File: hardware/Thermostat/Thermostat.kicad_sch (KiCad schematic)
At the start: 54 parts, among them J1 Barrel_Jack_Switch, J2 Screw_Terminal_01x02, J3 AVR-ISP-6, J4 MainConnectorr, K1 G6E, K2 G6E, K3 G6E, K4 G6E, SW1 12MM, SW2 12MM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

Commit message: WIP
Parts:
- removed BT1: Battery_Cell, Battery:BatteryHolder_Keystone_1058_1x2032, symbol Device:Battery_Cell
- removed C7, C8: 0.1uF, Capacitor_SMD:C_0603_1608Metric, symbol Device:C
- removed J2: Screw_Terminal_01x02, TerminalBlock_MetzConnect:TerminalBlock_MetzConnect_Type094_RT03502HBLU_1x02_P5.00mm_Horizontal, symbol Connector:Screw_Terminal_01x02
- removed U7: THVD1500, Package_SO:SOIC-8_3.9x4.9mm_P1.27mm, symbol Interface_UART:THVD1500
- added J2: Conn_01x02_Pin, Connector_PinHeader_2.54mm:PinHeader_1x02_P2.54mm_Vertical_SMD_Pin1Left, symbol Connector:Conn_01x02_Pin
- added U2: 47L04, Package_SO:SOIC-8_3.9x4.9mm_P1.27mm, symbol Memory_NVRAM:47L04
- Y1: footprint Crystal:Crystal_SMD_HC49-SD -> Crystal:Crystal_SMD_5032-2Pin_5.0x3.2mm
- Y2: footprint ThermostatFootprints:MC-306_EPS -> Crystal:Crystal_SMD_5032-2Pin_5.0x3.2mm
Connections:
- net +BATT is gone; now on net +5V: U8.8 (VCC)
- net +5V: no longer U8.3 (VBAT)
- net GND: now also SW2.1, U8.3 (VBAT); no longer SW2.2
- net RX0: now also J2.2 (Pin_2)
- net TX0: now also J2.1 (Pin_1)
- net at U5.32 (PD2): now also SW2.2; no longer SW2.1
- no-connect marks 20 -> 18

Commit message: Wip
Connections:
- net at D4.2 (A), U3.4 (IN4): now also U5.22 (ADC7); no longer U5.14 (PB2)
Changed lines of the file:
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@@
-	)
-	(no_connect
-		(at 20.32 118.11)
 	)
 	(no_connect
@@
 	)
 	(no_connect
+		(at 50.8 115.57)
+	)
+	(no_connect
 		(at 50.8 110.49)
 	)
@@
 	(wire
 		(pts
+			(xy 16.51 90.17) (xy 16.51 118.11)
+		)
+		(stroke
+			(width 0)
+			(type default)
+		)
+	)
+	(wire
+		(pts
 			(xy 50.8 190.5) (xy 64.77 190.5)
 		)
@@
 	(wire
 		(pts
-			(xy 64.77 115.57) (xy 50.8 115.57)
+			(xy 16.51 118.11) (xy 20.32 118.11)
 		)
 		(stroke
@@
 	(wire
 		(pts
+			(xy 45.72 101.6) (xy 45.72 90.17)
+		)
+		(stroke
+			(width 0)
+			(type default)
+		)
+	)
+	(wire
+		(pts
 			(xy 193.04 29.21) (xy 209.55 29.21)
 		)
@@
 	(wire
 		(pts
+			(xy 64.77 101.6) (xy 64.77 138.43)
+		)
+		(stroke
+			(width 0)
+			(type default)
+		)
+	)
+	(wire
+		(pts
 			(xy 195.58 104.14) (xy 195.58 95.25)
 		)
@@
 	(wire
 		(pts
-			(xy 64.77 138.43) (xy 64.77 115.57)
-		)
-		(stroke
-			(width 0)
-			(type default)
-		)
-	)
-	(wire
-		(pts
 			(xy 158.75 77.47) (xy 158.75 82.55)
 		)
@@
 	(wire
 		(pts
+			(xy 64.77 101.6) (xy 45.72 101.6)
+		)
+		(stroke
+			(width 0)
+			(type default)
+		)
+	)
+	(wire
+		(pts
 			(xy 93.98 111.76) (xy 93.98 115.57)
 		)
@@
 		(pts
 			(xy 229.87 26.67) (xy 259.08 26.67)
+		)
+		(stroke
+			(width 0)
+			(type default)
+		)
+	)
+	(wire
+		(pts
+			(xy 45.72 90.17) (xy 16.51 90.17)
 		)
 		(stroke
@@
 			(justify left bottom)
 		)
-		(property "Netclass" "Power"
+		(property "Netclass" "MegaPower"
 			(at 146.7485 58.42 0)
 			(effects
@@
 			(justify left bottom)
 		)
-		(property "Netclass" "Power"
+		(property "Netclass" "MegaPower"
 			(at 128.9685 53.34 0)
 			(effects
@@
 			(justify left bottom)
 		)
-		(property "Netclass" "Power"
+		(property "Netclass" "MegaPower"
 			(at 137.8585 55.88 0)
 			(effects
@@
 			(justify left bottom)
 		)
-		(property "Netclass" "Power"
+		(property "Netclass" "MegaPower"
 			(at 126.4285 63.5 0)
 			(effects

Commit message: WIP
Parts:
- removed D1, D2, D3, D4: LED, LED_SMD:LED_0805_2012Metric, symbol Device:LED
- removed D5: SM6T27A, Diode_SMD:D_SMB, symbol Diode:SM6T27A
- removed R2, R3, R4, R5: 660, Resistor_SMD:R_0603_1608Metric, symbol Device:R_US
- removed S1: 2MS1T1B1M2QES, ThermostatFootprints:2MS1T1B1M2QES, symbol ThermoSymbols:2MS3T1B1M2QES
- removed S3: 2MS1T1B1M2QES, ThermostatFootprints:2MS1T1B1M2QES, symbol ThermoSymbols:2MS1T1B1M2QES
- removed Y2: Crystal_GND23, Crystal:Crystal_SMD_5032-2Pin_5.0x3.2mm, symbol Device:Crystal_GND23
- added C7: C, Capacitor_SMD:C_0603_1608Metric, symbol Device:C
- added D5: 1N4007, Diode_THT:D_DO-41_SOD81_P10.16mm_Horizontal, symbol Diode:1N4007
- added SW7, SW9: 12MM, ThermostatFootprints:B3F, symbol Switch:SW_Push
- added Y3: Crystal, Crystal:Crystal_SMD_5032-2Pin_5.0x3.2mm, symbol Device:Crystal
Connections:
- net +5V: now also U1.6 (^RESET), U2.8 (VCC)
- net 24VDC: now also D5.1 (K); no longer J1.1
- net GND: now also U2.2 (A1), U2.3 (A2), U2.4 (VSS), C7.2, SW7.2, SW9.2
- net I2C_SCL: now also U2.6 (SCL)
- net I2C_SDA: now also U2.5 (SDA)
- net ^RESET: no longer U1.6 (^RESET)
- net at U8.1 (X1): now also Y3.2
- net at U8.2 (X2): now also Y3.1
- net at SW3.1: now also U5.9 (PD5); no longer U5.11 (PD7)
- net at U2.1 (VCAP): now also C7.1
- net at U5.10 (PD6): now also SW9.1
- net at K1.1: now also U3.13 (OUT4); no longer U3.16 (OUT1)
- net at K2.1: now also U3.14 (OUT3); no longer U3.15 (OUT2)
- net at K3.1: now also U3.15 (OUT2); no longer U3.14 (OUT3)
- net at K4.1: now also U3.16 (OUT1); no longer U3.13 (OUT4)
- new net: D5.2 (A), J1.1
- new net: SW7.1, U5.11 (PD7)
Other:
- note added: "FAN ON/AUTO"
- note added: "HEAT/COOL"
- note added: "SELECT"
- note removed: "COOL"
- note removed: "FAN ON"
- note removed: "HEAT"
- note removed: "Should be 2MS3T1B1M2QES"
- moved on the sheet: C9, H1, H2, H3, H4, R1, R6, R7, SW3, SW5, U1, U2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

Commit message: WIP
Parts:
- removed U6: TMP116xxDRV, Package_SON:WSON-6-1EP_2x2mm_P0.65mm_EP1x1.6mm_ThermalVias, symbol Sensor_Temperature:TMP116xxDRV
- added C10, C8: 0.1uF, Capacitor_SMD:C_0603_1608Metric, symbol Device:C
- added U9: SHT4x, Sensor_Humidity:Sensirion_DFN-4_1.5x1.5mm_P0.8mm_SHT4x_NoCentralPad, symbol Sensor_Humidity:SHT4x
- C7: value C -> 6.8uF
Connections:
- net +5V: now also C9.2, C10.1, C8.2, U9.3 (VDD); no longer C9.1
- net GND: now also C9.1, C10.2, C8.1, U9.4 (VSS); no longer C9.2
- net I2C_SCL: now also U9.2 (SCL)
- net I2C_SDA: now also U9.1 (SDA)
- no-connect marks 18 -> 17

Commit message: Wiring / DRC / JLCPCB
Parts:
- removed U5: ATmega88-20A, Package_QFP:TQFP-32_7x7mm_P0.8mm, symbol MCU_Microchip_ATmega:ATmega88-20A
- added U5: ATmega168P-20A, Package_QFP:TQFP-32_7x7mm_P0.8mm, symbol MCU_Microchip_ATmega:ATmega168P-20A
- C1, C2, C3: footprint Capacitor_SMD:C_0603_1608Metric -> Capacitor_SMD:C_1808_4520Metric
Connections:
- net +5V: now also U5.4 (VCC), U5.6 (VCC)
- net GND: now also U5.18 (AVCC), U5.20 (AREF), U5.21 (GND), U5.3 (GND), U5.5 (GND)
- net I2C_SCL: now also U5.28 (PC5)
- net I2C_SDA: now also U5.27 (PC4)
- net RX0: now also U5.30 (PD0)
- net TX0: now also U5.31 (PD1)
- net ^RESET: now also U5.29 (~{RESET}/PC6)
- net at SW3.1: now also U5.9 (PD5)
- net at C4.2, Y1.2: now also U5.7 (XTAL1/PB6)
- net at SW4.1: now also U5.26 (PC3)
- net at C5.2, Y1.1: now also U5.8 (XTAL2/PB7)
- net at SW1.1: now also U5.1 (PD3)
- net at SW9.1: now also U5.10 (PD6)
- net at SW7.1: now also U5.11 (PD7)
- net at J3.4 (MOSI): now also U5.15 (PB3)
- net at J3.1 (MISO): now also U5.16 (PB4)
- net at J3.3 (SCK): now also U5.17 (PB5)
- net at U3.4 (IN4): now also U5.14 (PB2)
- net at U3.3 (IN3): now also U5.23 (PC0)
- net at U3.2 (IN2): now also U5.24 (PC1)
- net at U3.1 (IN1): now also U5.25 (PC2)
- net at SW2.2: now also U5.32 (PD2)
- net SCREEN_BUSY renamed SCBUSY
- net SCBUSY: now also U5.13 (PB1)
- no-connect marks 17 -> 16
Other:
- moved on the sheet: U1

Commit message: Some labels
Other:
- note added: "HEAT/COOL/NONE"
- note removed: "HEAT/COOL"
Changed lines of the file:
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@@
 		)
 	)
-	(text "HEAT/COOL"
+	(text "HEAT/COOL/NONE"
 		(exclude_from_sim no)
-		(at 85.852 166.878 0)
+		(at 89.408 166.878 0)
 		(effects
 			(font
@@
 	(text "FAN ON/AUTO"
 		(exclude_from_sim no)
-		(at 90.678 171.704 0)
+		(at 86.868 171.45 0)
 		(effects
 			(font

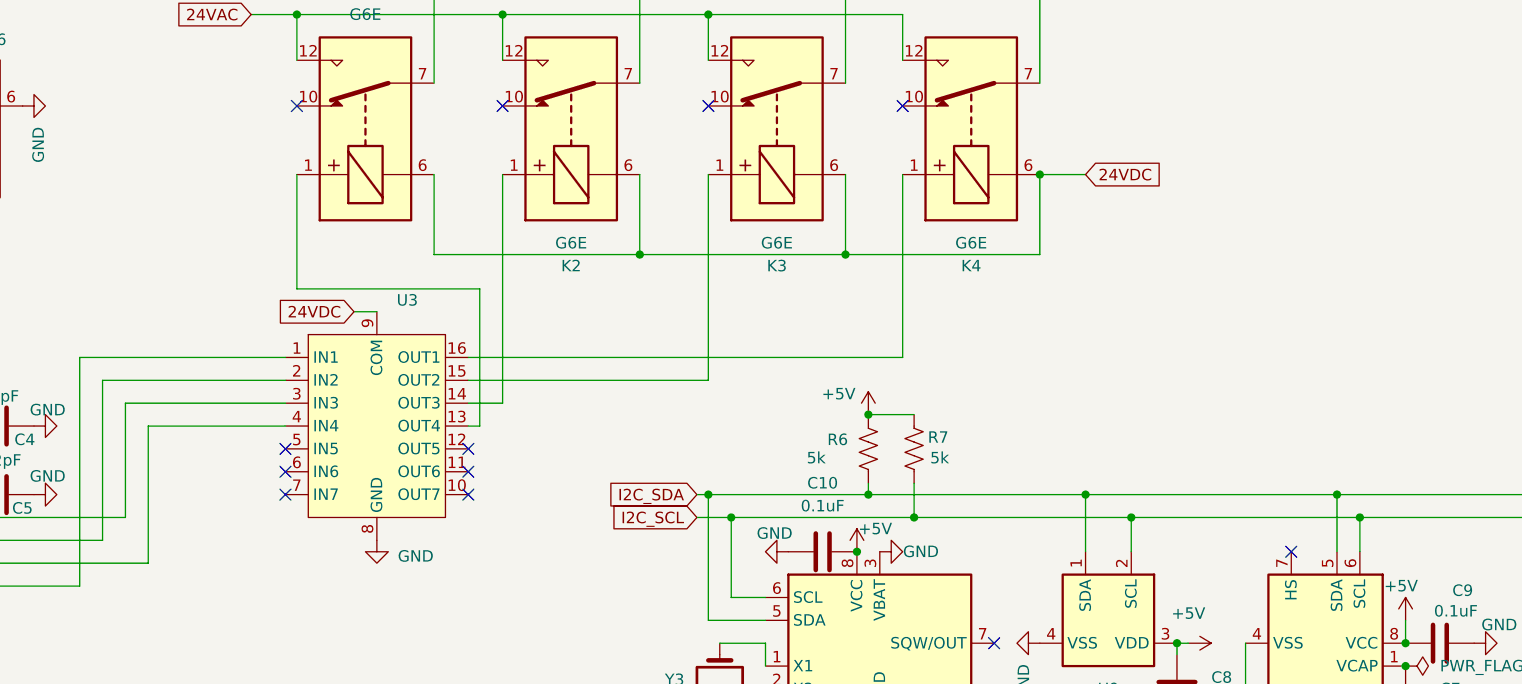
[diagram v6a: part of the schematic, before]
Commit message: Realize from real-world experiment that relay coils are directional, and fix
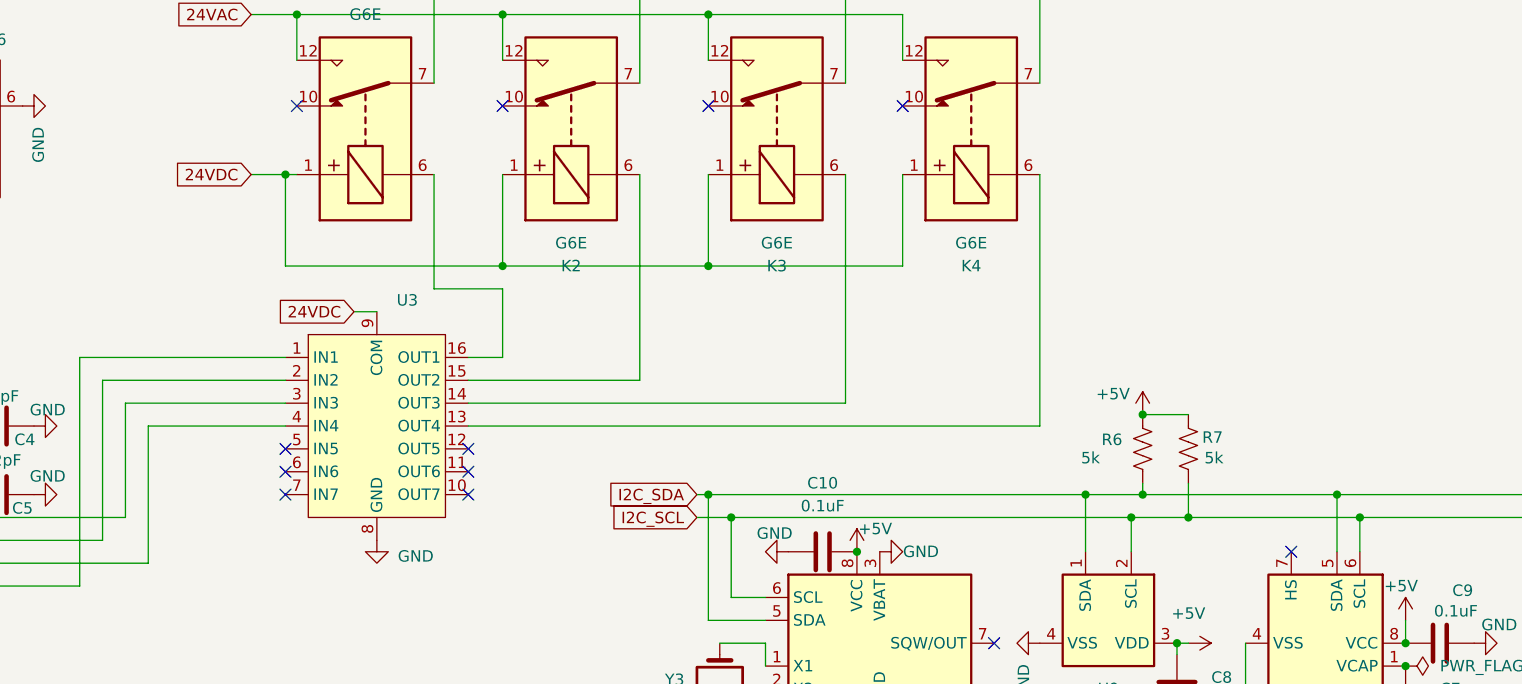
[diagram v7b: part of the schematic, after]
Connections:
- net 24VDC: now also K1.1, K2.1, K3.1, K4.1; no longer K1.6, K2.6, K3.6, K4.6
- net at U3.13 (OUT4): now also K4.6; no longer K1.1
- net at U3.14 (OUT3): now also K3.6; no longer K2.1
- net at U3.15 (OUT2): now also K2.6; no longer K3.1
- net at U3.16 (OUT1): now also K1.6; no longer K4.1
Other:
- moved on the sheet: R6, R7

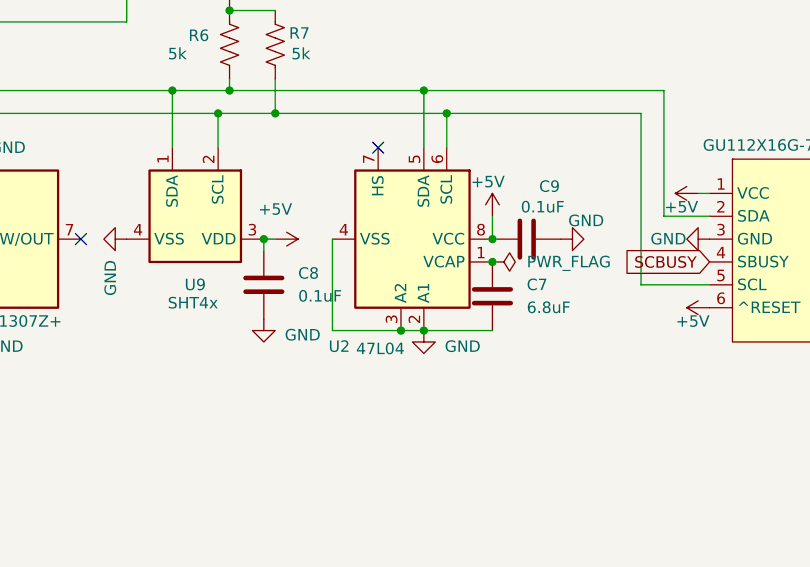
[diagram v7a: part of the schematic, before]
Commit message: Integrate 47L04
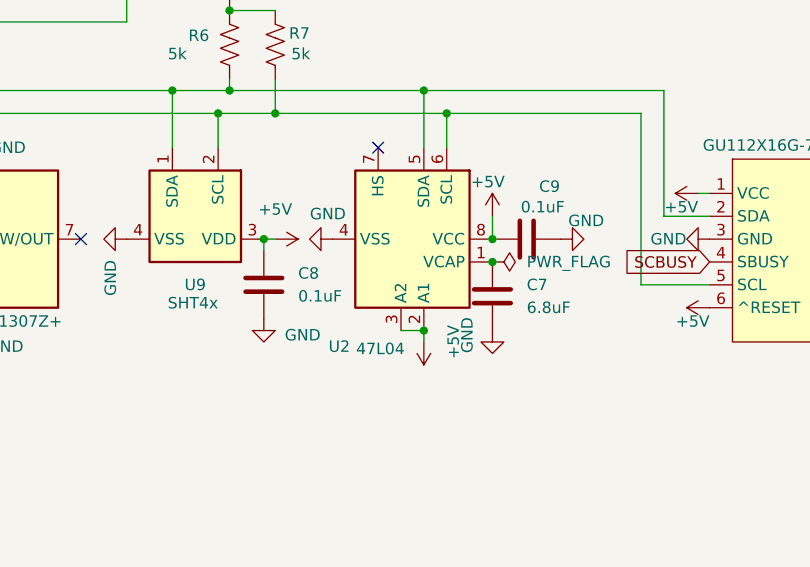
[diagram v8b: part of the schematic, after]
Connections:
- net +5V: now also U2.2 (A1), U2.3 (A2)
- net GND: no longer U2.2 (A1), U2.3 (A2)
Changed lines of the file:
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@@
 	)
 	(junction
+		(at 228.6 157.48)
+		(diameter 0)
+		(color 0 0 0 0)
+	)
+	(junction
 		(at 190.5 35.56)
 		(diameter 0)
@@
 	)
 	(junction
-		(at 228.6 157.48)
-		(diameter 0)
-		(color 0 0 0 0)
-	)
-	(junction
 		(at 76.2 130.81)
 		(diameter 0)
@@
 	)
 	(junction
-		(at 226.06 157.48)
-		(diameter 0)
-		(color 0 0 0 0)
-	)
-	(junction
 		(at 236.22 147.32)
 		(diameter 0)
@@
 	(wire
 		(pts
-			(xy 218.44 147.32) (xy 218.44 157.48)
-		)
-		(stroke
-			(width 0)
-			(type default)
-		)
-	)
-	(wire
-		(pts
 			(xy 158.75 130.81) (xy 200.66 130.81)
 		)
@@
 	(wire
 		(pts
-			(xy 228.6 157.48) (xy 236.22 157.48)
-		)
-		(stroke
-			(width 0)
-			(type default)
-		)
-	)
-	(wire
-		(pts
 			(xy 50.8 120.65) (xy 67.31 120.65)
 		)
@@
 	(wire
 		(pts
-			(xy 218.44 157.48) (xy 226.06 157.48)
-		)
-		(stroke
-			(width 0)
-			(type default)
-		)
-	)
-	(wire
-		(pts
 			(xy 88.9 63.5) (xy 93.98 63.5)
 		)
@@
 	(wire
 		(pts
+			(xy 228.6 157.48) (xy 228.6 158.75)
+		)
+		(stroke
+			(width 0)
+			(type default)
+		)
+	)
+	(wire
+		(pts
 			(xy 116.84 40.64) (xy 116.84 35.56)
 		)
@@
 		(on_board yes)
 		(dnp no)
-		(fields_autoplaced yes)
 		(property "Reference" "C8"
 			(at 214.63 151.1299 0)
@@
 	)
 	(symbol
+		(lib_id "power:+5V")
+		(at 228.6 158.75 180)
+		(unit 1)
+		(exclude_from_sim no)
+		(in_bom yes)
+		(on_board yes)
+		(dnp no)
+		(property "Reference" "#PWR031"
+			(at 228.6 154.94 0)
+			(effects
+				(font
+					(size 1.27 1.27)
+				)
+				(hide yes)
+			)
+		)
+		(property "Value" "+5V"
+			(at 231.902 158.75 90)
+			(effects
+				(font
+					(size 1.27 1.27)
+				)
+			)
+		)
+		(property "Footprint" ""
+			(at 228.6 158.75 0)
+			(effects
+				(font
+					(size 1.27 1.27)
+				)
+				(hide yes)
+			)
+		)
+		(property "Datasheet" ""
+			(at 228.6 158.75 0)
+			(effects
+				(font
+					(size 1.27 1.27)
+				)
+				(hide yes)
+			)
+		)
+		(property "Description" "Power symbol creates a global label with name \"+5V\""
+			(at 228.6 158.75 0)
+			(effects
+				(font
+					(size 1.27 1.27)
+				)
+				(hide yes)
+			)
+		)
+		(pin "1"
+		)
+		(instances
+			(project "Thermostat"
+				(path "/dae3c193-ffe6-4911-a810-cfe956c95f3b"
+					(reference "#PWR031")
+					(unit 1)
+				)
+			)
+		)
+	)
+	(symbol
 		(lib_id "power:GND")
 		(at 82.55 87.63 90)
@@
 	)
 	(symbol
+		(lib_id "power:GND")
+		(at 236.22 157.48 0)
+		(unit 1)
+		(exclude_from_sim no)
+		(in_bom yes)
+		(on_board yes)
+		(dnp no)
+		(property "Reference" "#PWR029"
+			(at 236.22 163.83 0)
+			(effects
+				(font
+					(size 1.27 1.27)
+				)
+				(hide yes)
+			)
+		)
+		(property "Value" "GND"
+			(at 233.426 157.988 90)
+			(effects
+				(font
+					(size 1.27 1.27)
+				)
+			)
+		)
+		(property "Footprint" ""
+			(at 236.22 157.48 0)
+			(effects
+				(font
+					(size 1.27 1.27)
+				)
+				(hide yes)
+			)
+		)
+		(property "Datasheet" ""
+			(at 236.22 157.48 0)
+			(effects
+				(font
+					(size 1.27 1.27)
+				)
+				(hide yes)
+			)
+		)
+		(property "Description" "Power symbol creates a global label with name \"GND\" , ground"
+			(at 236.22 157.48 0)
+			(effects
+				(font
+					(size 1.27 1.27)
+				)
+				(hide yes)
+			)
+		)
+		(pin "1"
+		)
+		(instances
+			(project "Thermostat"
+				(path "/dae3c193-ffe6-4911-a810-cfe956c95f3b"
+					(reference "#PWR029")
+					(unit 1)
+				)
+			)
+		)
+	)
+	(symbol
 		(lib_id "Regulator_Linear:UA78M05QDCYRQ1")
 		(at 152.4 30.48 0)
@@
 	(symbol
 		(lib_id "power:GND")
-		(at 228.6 157.48 0)
+		(at 218.44 147.32 270)
 		(unit 1)
 		(exclude_from_sim no)
@@
 		(dnp no)
 		(property "Reference" "#PWR03"
-			(at 228.6 163.83 0)
+			(at 212.09 147.32 0)
 			(effects
 				(font
@@
 		)
 		(property "Value" "GND"
-			(at 232.918 159.258 0)
+			(at 217.932 144.526 90)
 			(effects
 				(font
@@
 		)
 		(property "Footprint" ""
-			(at 228.6 157.48 0)
+			(at 218.44 147.32 0)
 			(effects
 				(font
@@
 		)
 		(property "Datasheet" ""
-			(at 228.6 157.48 0)
+			(at 218.44 147.32 0)
 			(effects
 				(font
@@
 		)
 		(property "Description" "Power symbol creates a global label with name \"GND\" , ground"
-			(at 228.6 157.48 0)
+			(at 218.44 147.32 0)
 			(effects
 				(font
